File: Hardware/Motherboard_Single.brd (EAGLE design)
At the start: 86.4 x 73.7 mm, 74 parts, among them J1 MICROMOD-2222-C, J10 MICRO-SD-PUSH-PUSH-EXT-PIN, J2 Vertical Qwiic Connector, J4 QWIIC_RIGHT_ANGLE, J5 CORTEX_JTAG_DEBUG_MINIMUM_PTH, J6 MICROMOD_CARRIER, U2 MCP73831, U5 AP7361C-33

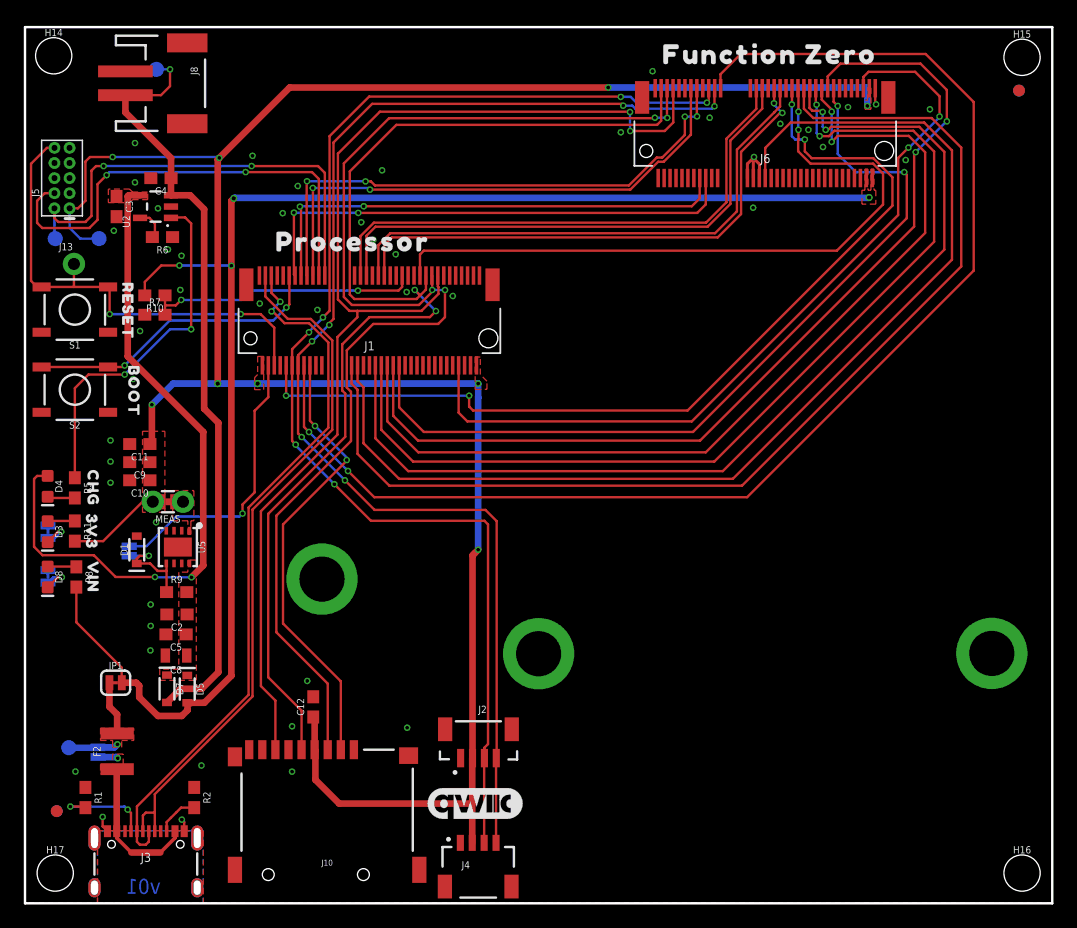
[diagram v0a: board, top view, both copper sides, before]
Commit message: Adds another standoff for qwiic boards around the lower left edge, adds silk
* Removes jumper for "VIN/VUSB"
* Correctly routes USB_VIN on processor connector to VIN
* Double routes PWR_EN for ESP32 Processor boards
* Moves SD Card up 0.04"
* Adds more measures
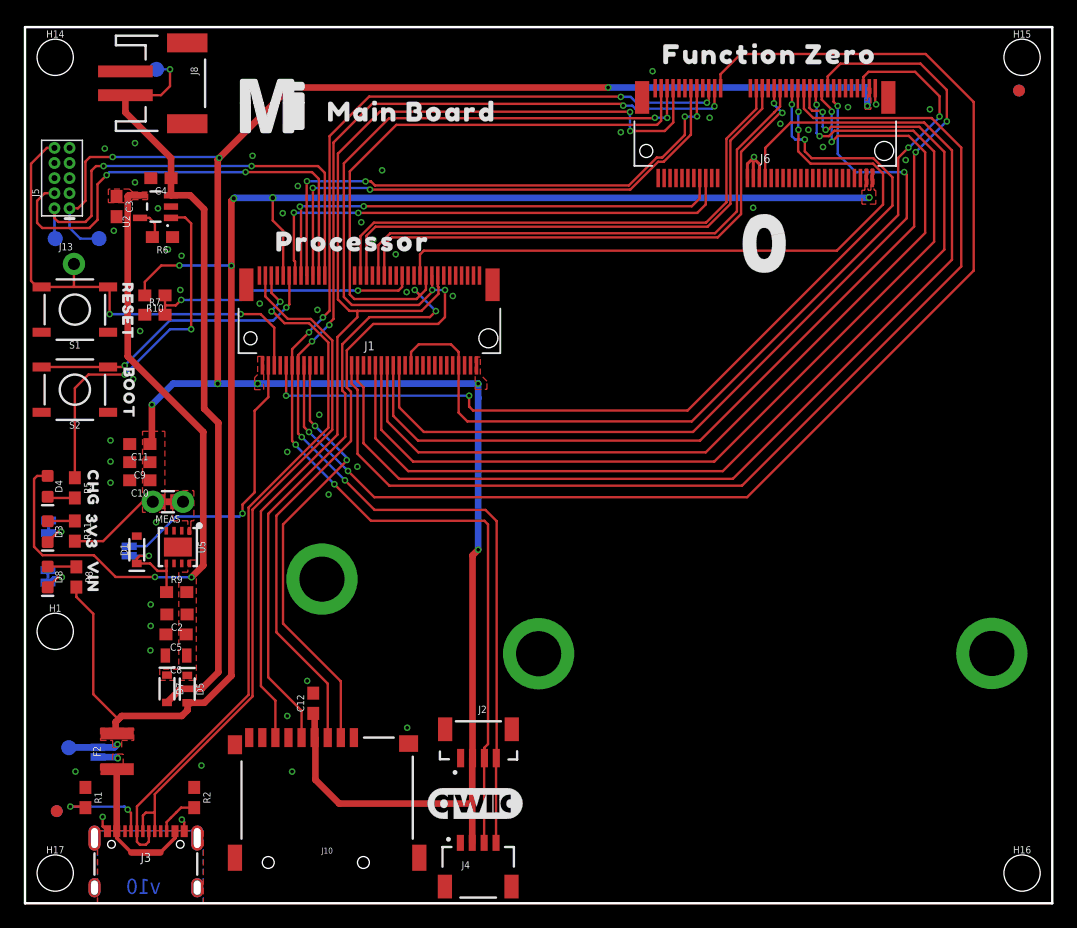
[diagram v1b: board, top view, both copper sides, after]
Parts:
- removed JP1: JUMPER-SMT_2_NC_TRACE_SILK, SparkFun-Jumpers:SMT-JUMPER_2_NC_TRACE_SILK
- added H1: STAND-OFFTIGHT, SparkFun-Hardware:STAND-OFF-TIGHT
- added U$12: (no value), SparkFun-MicroMod:MICROMOD_MI_LOGO_1
- added U$13: (no value), top:0525
- added U$14: (no value), top:MAIN_BOARD522
- added U$15: (no value), top:MAIN523
- added U$16: (no value), top:BOARD524
- moved U$7 4.99 mm to (5.38, 27.5), turned to 0 degrees
- moved U$6 4.93 mm to (5.59, 31.8), turned to 0 degrees
- moved U$11 4.67 mm to (12.0, 29.7), turned to 0 degrees
- moved U$8 3.38 mm to (8.53, 12.8), turned to 0 degrees
- moved J10 1.02 mm to (25.4, 3.43)
- moved U$9 0.43 mm to (8.74, 42.9)
- moved 3V3_LED 0.41 mm to (1.98, 31.6)
- moved C12 0.30 mm to (24.2, 16.8)
- moved H14 0.18 mm to (2.54, 71.1)
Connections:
- removed net USB_VIN: J1.9
- removed net V_USB: BYP.2, F2.2, JP1.1, TP4.1
- net PWR_EN0: now also J1.52
- net VIN: now also BYP.2, F2.2, J1.9, TP4.1; no longer JP1.2
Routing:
- net VIN: track 125.0 -> 139.1 mm, vias 4 -> 6
- net V_USB: track 8.74 -> 0.00 mm, vias 1 -> 0
- net PWR_EN0: track 68.3 -> 75.0 mm
- net SPI_PROCESSOR_SDO: track 102.9 -> 101.9 mm
- net D1-PROCESSOR/SD_CARD_!CS!: track 37.8 -> 36.8 mm
- net SPI_PROCESSOR_SDI: track 98.4 -> 97.4 mm
- net SPI_PROCESSOR_SCK: track 99.3 -> 98.3 mm
- net GND: vias 47 -> 52
- removed copper zone on layer 1, net V_USB
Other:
- board text added: "v10"
- board text removed: "v01"

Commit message: Adds 2 pin dip switch for charge selection, adds PCHAN MOSFET to VBATT net
* Adds better silk
* Moves stuff around schematic for better clarity
* Adds charge table to schematic
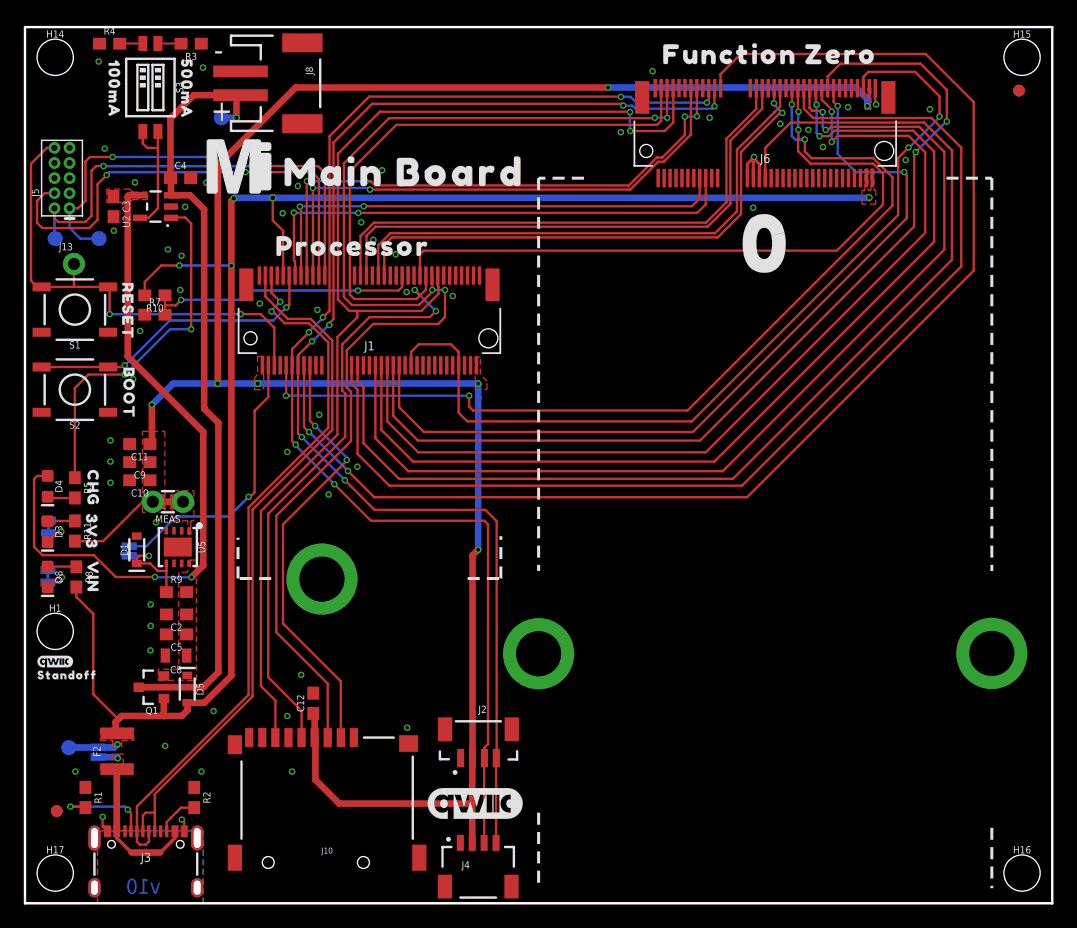
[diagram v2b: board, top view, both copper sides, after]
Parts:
- removed D7: 3A/10V/280mV, SparkFun-DiscreteSemi:SOD-323
- removed R6: 2.0k, SparkFun-Resistors:0603
- added Q1: 20V/4.2A/52mΩ/1.4W, SparkFun-DiscreteSemi:SOT23-3
- added R3: 2.0k, SparkFun-Resistors:0603
- added R4: 10k, SparkFun-Resistors:0603
- added S3: DIP-02-SMD-50MIL, SparkFun-Switches:DIPSWITCH-02-50MIL
- added U$17: (no value), top:100MA6
- added U$18: (no value), top:500MA101
- added U$19: (no value), top:MAIN_BOARD5523
- added U$20: (no value), SparkFun-Aesthetics:QWIIC_3MM
- added U$21: (no value), top:STANDOFF501
- LOGO3: value OSHW-LOGOMINI -> OSHW-LOGOL; device SparkFun-Aesthetics:OSHW-LOGO-MINI -> SparkFun-Aesthetics:OSHW-LOGO-L
- U$14: device top:MAIN_BOARD522 -> SparkFun-MicroMod:MICROMOD_LOGO_1
- moved U$14 51.0 mm to (59.8, 23.5), flipped to the bottom
- moved J8 9.68 mm to (21.8, 68.9)
- moved U$16 8.64 mm to (54.4, 16.8)
- moved U$15 8.54 mm to (66.3, 16.9)
- moved TP3 6.81 mm to (16.5, 66.0)
- moved U$12 5.80 mm to (18.0, 62.0)
- moved LOGO3 2.17 mm to (81.8, 8.38)
- moved C4 1.65 mm to (13.1, 61.0), turned to 0 degrees
- moved U$5 0.38 mm to (27.6, 55.2)
- moved C3 0.25 mm to (7.44, 58.6)
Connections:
- new net N$11: R4.2, S3.2
- new net N$7: R3.2, S3.1
- net GND: now also R3.1, R4.1; no longer R6.1
- net N$8: now also S3.3, S3.4; no longer R6.2
- net VCC: now also Q1.2; no longer D7.C
- net VIN: now also Q1.1
- net V_BATT: now also Q1.3; no longer D7.A
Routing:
- net N$8: track 2.68 -> 11.2 mm
- net N$11: track 0.00 -> 1.95 mm
- net N$7: track 0.00 -> 1.95 mm
- net V_BATT: track 64.7 -> 66.4 mm
- net VIN: track 139.1 -> 140.6 mm
- net 3.3V: track 196.3 -> 195.7 mm
- net GND: vias 52 -> 56
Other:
- board text added: "+"
- board text added: "-"

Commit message: Replaces MOSFET with another one
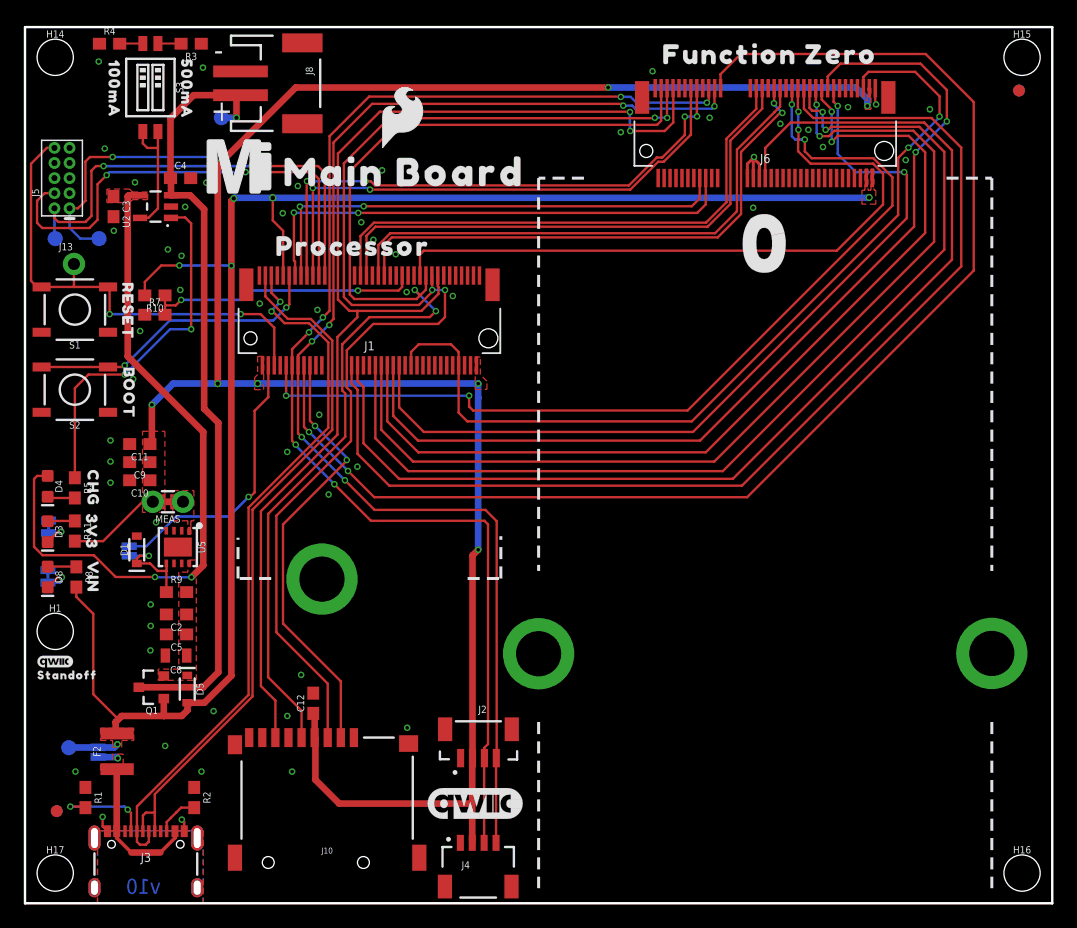
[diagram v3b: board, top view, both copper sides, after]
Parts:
- added U$22: (no value), SparkFun-Aesthetics:SFE_LOGO_FLAME_.2
- Q1: value 20V/4.2A/52mΩ/1.4W -> 3.1A/30V/105mΩ
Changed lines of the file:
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@@
 <wire x1="77.47" y1="60.96" x2="81.28" y2="60.96" width="0.254" layer="21" style="shortdash"/>
 <wire x1="81.28" y1="60.96" x2="81.28" y2="27.94" width="0.254" layer="21" style="shortdash"/>
-<wire x1="81.28" y1="6.35" x2="81.28" y2="1.27" width="0.254" layer="21" style="shortdash"/>
-<wire x1="43.18" y1="7.62" x2="43.18" y2="1.27" width="0.254" layer="21" style="shortdash"/>
+<wire x1="81.28" y1="15.24" x2="81.28" y2="1.27" width="0.254" layer="21" style="shortdash"/>
+<wire x1="43.18" y1="15.24" x2="43.18" y2="1.27" width="0.254" layer="21" style="shortdash"/>
 <wire x1="20.701" y1="27.305" x2="17.907" y2="27.305" width="0.254" layer="21" style="shortdash"/>
 <wire x1="17.907" y1="27.305" x2="17.907" y2="30.734" width="0.254" layer="21" style="shortdash"/>
@@
 <attribute name="VALUE" x="7.112" y="71.501" size="0.6096" layer="27" font="vector" ratio="20" align="top-center"/>
 </element>
-<element name="Q1" library="SparkFun-DiscreteSemi" package="SOT23-3" value="20V/4.2A/52mΩ/1.4W" x="10.668" y="18.161" smashed="yes" rot="R90">
+<element name="Q1" library="SparkFun-DiscreteSemi" package="SOT23-3" value="3.1A/30V/105mΩ" x="10.668" y="18.161" smashed="yes" rot="R90">
 <attribute name="NAME" x="10.668" y="16.51" size="0.6096" layer="25" font="vector" ratio="20" rot="R180" align="bottom-center"/>
-<attribute name="PROD_ID" value="TRANS-14388" x="8.128" y="18.161" size="1.778" layer="27" rot="R90" display="off"/>
-<attribute name="VALUE" x="10.668" y="19.812" size="0.6096" layer="27" font="vector" ratio="20" rot="R180" align="top-center"/>
+<attribute name="PROD_ID" value="TRANS-11308" x="8.128" y="18.161" size="1.778" layer="27" rot="R90" display="off"/>
+<attribute name="VALUE" value="3.1A/30V/105mΩ" x="10.668" y="19.812" size="0.6096" layer="27" font="vector" ratio="20" rot="R180" align="top-center"/>
 </element>
 <element name="U$17" library="top" package="100MA6" value="" x="7.493" y="68.453" smashed="yes" rot="R270"/>
@@
 <element name="U$20" library="SparkFun-Aesthetics" package="QWIIC_3MM" value="" x="2.54" y="20.32" smashed="yes"/>
 <element name="U$21" library="top" package="STANDOFF501" value="" x="3.556" y="19.177" smashed="yes"/>
+<element name="U$22" library="SparkFun-Aesthetics" package="SFE_LOGO_FLAME_.2" value="" x="31.75" y="66.04" smashed="yes"/>
 </elements>
 <signals>

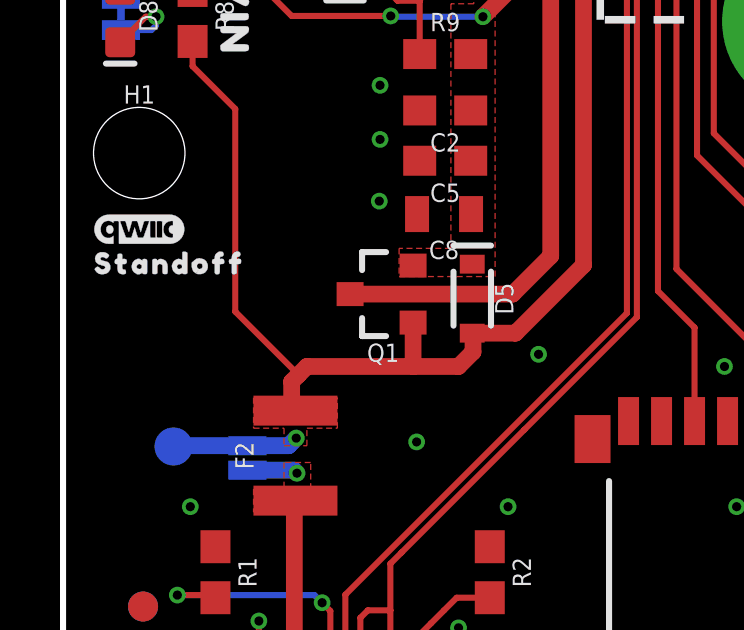
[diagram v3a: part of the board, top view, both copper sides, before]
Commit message: Adds 10k pulldown to gate on PCHAN MOSFET, fixes length measurement
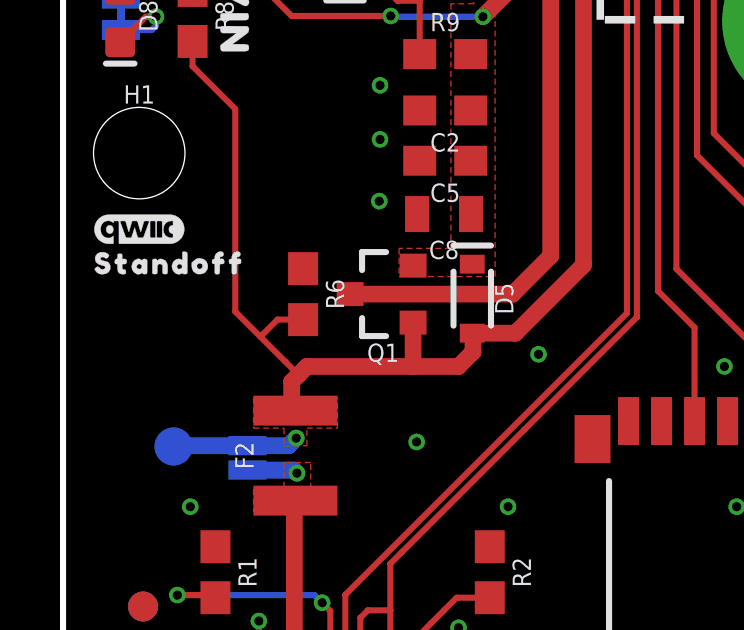
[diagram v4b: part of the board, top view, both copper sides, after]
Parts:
- added R6: 10k, SparkFun-Resistors:0603
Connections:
- net GND: now also R6.1
- net VIN: now also R6.2
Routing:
- net VIN: track 140.6 -> 142.4 mm
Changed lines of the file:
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@@
 <dimension x1="83.82" y1="2.54" x2="86.36" y2="2.54" x3="85.09" y3="-8.128" textsize="1.778" textratio="15" layer="47" unit="inch"/>
 <dimension x1="62.23" y1="63.246" x2="86.36" y2="63.246" x3="74.295" y3="76.454" textsize="1.778" textratio="15" layer="47" unit="inch"/>
-<dimension x1="0" y1="73.66" x2="61.976" y2="73.66" x3="30.988" y3="76.962" textsize="1.778" textratio="15" layer="47" unit="inch"/>
+<dimension x1="0" y1="73.66" x2="62.23" y2="73.66" x3="31.115" y3="76.962" textsize="1.778" textratio="15" layer="47" unit="inch"/>
 <text x="15.621" y="65.786" size="1.778" layer="21" font="vector" ratio="15">+</text>
 <text x="15.875" y="70.866" size="1.778" layer="21" font="vector" ratio="15">-</text>
@@
 <element name="U$21" library="top" package="STANDOFF501" value="" x="3.556" y="19.177" smashed="yes"/>
 <element name="U$22" library="SparkFun-Aesthetics" package="SFE_LOGO_FLAME_.2" value="" x="31.75" y="66.04" smashed="yes"/>
+<element name="R6" library="SparkFun-Resistors" package="0603" value="10k" x="8.001" y="18.161" smashed="yes" rot="R270">
+<attribute name="NAME" x="8.763" y="18.161" size="0.6096" layer="25" font="vector" ratio="20" rot="R270" align="bottom-center"/>
+<attribute name="PROD_ID" value="RES-00824" x="8.001" y="18.161" size="1.778" layer="27" font="vector" ratio="15" rot="R270" display="off"/>
+<attribute name="VALUE" x="7.239" y="18.161" size="0.6096" layer="27" font="vector" ratio="20" rot="R270" align="top-center"/>
+</element>
 </elements>
 <signals>
@@
 <via x="14.8336" y="11.0744" extent="1-16" drill="0.3048"/>
 <via x="15.8496" y="16.1544" extent="1-16" drill="0.3048"/>
+<contactref element="R6" pad="1"/>
 </signal>
 <signal name="V_BATT" class="1">
@@
 <wire x1="7.62" y1="14.4032" x2="7.747" y2="14.2762" width="0.5588" layer="1"/>
 <wire x1="4.318" y1="26.582" x2="4.318" y2="25.7556" width="0.2032" layer="1"/>
-<wire x1="5.7404" y1="17.5768" x2="7.8486" y2="15.4686" width="0.2032" layer="1"/>
+<wire x1="7.8486" y1="15.4686" x2="7.4041" y2="15.9131" width="0.2032" layer="1"/>
 <wire x1="4.318" y1="25.7556" x2="5.7404" y2="24.3332" width="0.2032" layer="1"/>
 <wire x1="5.7404" y1="24.3332" x2="5.7404" y2="17.5768" width="0.2032" layer="1"/>
@@
 <wire x1="11.668" y1="17.211" x2="11.668" y2="15.764" width="0.5588" layer="1"/>
 <wire x1="11.668" y1="15.764" x2="11.684" y2="15.748" width="0.5588" layer="1"/>
+<contactref element="R6" pad="2"/>
+<wire x1="8.001" y1="17.311" x2="7.874" y2="17.184" width="0.2032" layer="1"/>
+<wire x1="5.7404" y1="17.5768" x2="6.5786" y2="16.7386" width="0.2032" layer="1"/>
+<wire x1="6.5786" y1="16.7386" x2="7.4041" y2="15.9131" width="0.2032" layer="1"/>
+<wire x1="6.5786" y1="16.7386" x2="7.151" y2="17.311" width="0.2032" layer="1"/>
+<wire x1="7.151" y1="17.311" x2="8.001" y2="17.311" width="0.2032" layer="1"/>
 </signal>
 <signal name="SHLD">
